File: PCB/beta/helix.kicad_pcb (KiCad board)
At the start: 2 copper layers, 132 x 94 mm, 223 parts, among them J1 MJ-4PP-9, P1 CONN_01X01, P2 CONN_01X01, P3 OLED, P4 LED, P5 ICSP, SW1 SW_PUSH, SW10 SW_PUSH, SW11 SW_PUSH, SW12 SW_PUSH, SW13 SW_PUSH, SW14 SW_PUSH, SW15 SW_PUSH, SW16 SW_PUSH, SW17 SW_PUSH, SW18 SW_PUSH, SW19 SW_PUSH, SW2 SW_PUSH, SW20 SW_PUSH, SW21 SW_PUSH, SW22 SW_PUSH, SW23 SW_PUSH, SW24 SW_PUSH, SW25 SW_PUSH, SW26 SW_PUSH, SW27 SW_PUSH, SW28 SW_PUSH, SW29 SW_PUSH, SW3 SW_PUSH, SW30 SW_PUSH, SW31 SW_PUSH, SW32 SW_PUSH, SW33 Reset, SW4 SW_PUSH, SW5 SW_PUSH, SW6 SW_PUSH, SW7 SW_PUSH, SW8 SW_PUSH, SW9 SW_PUSH, U1 ProMicro, U10 SK6812mini, U11 SK6812mini, U12 SK6812mini, U13 SK6812mini, U14 SK6812mini, U15 SK6812mini, U16 SK6812mini, U17 SK6812mini, U18 SK6812mini, U19 SK6812mini, U2 SK6812mini, U20 SK6812mini, U21 SK6812mini, U22 SK6812mini, U23 SK6812mini, U24 SK6812mini, U25 SK6812mini, U26 SK6812mini, U27 SK6812mini, U28 SK6812mini, U29 SK6812mini, U3 SK6812mini, U30 SK6812mini, U31 SK6812mini, U32 SK6812mini, U33 SK6812mini, U4 SK6812mini, U5 SK6812mini, U6 SK6812mini, U7 SK6812mini, U8 SK6812mini, U9 SK6812mini

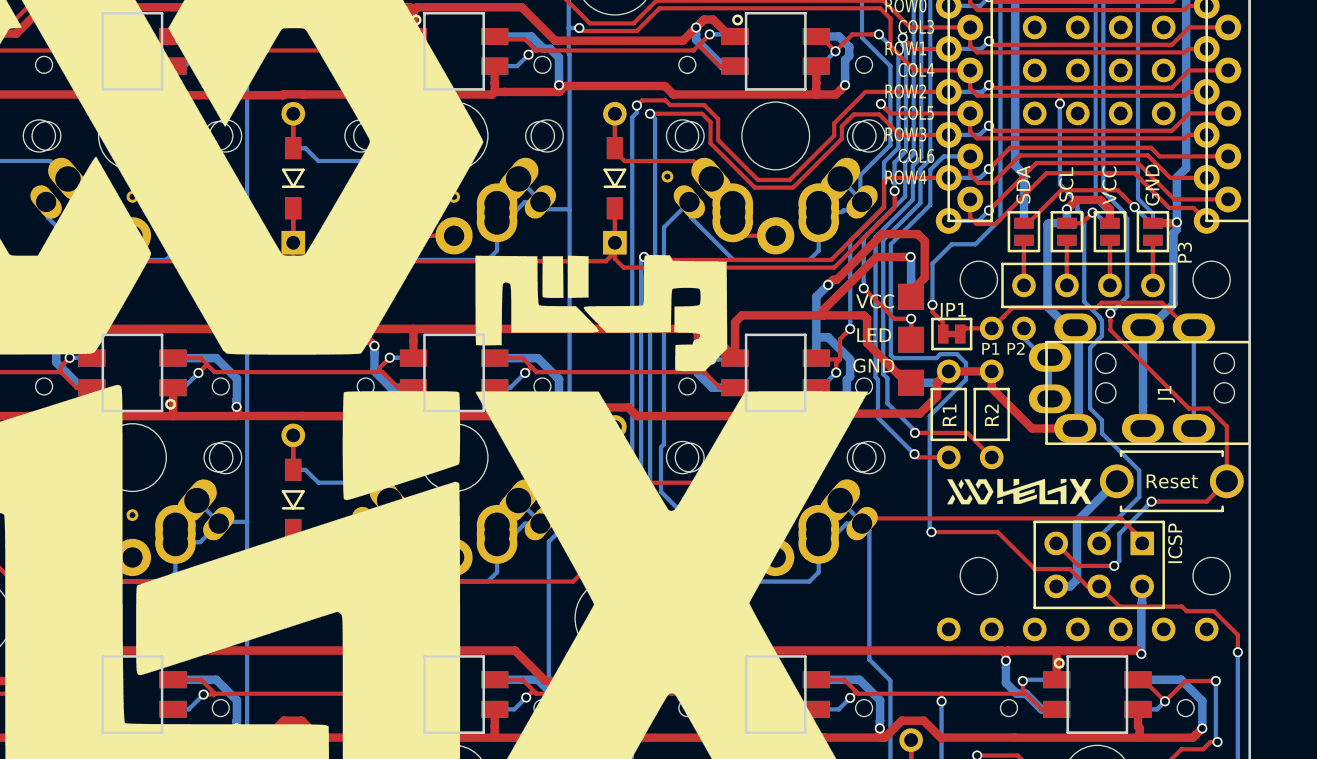
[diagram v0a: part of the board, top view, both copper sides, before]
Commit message: made changes to aux jack (now accepts generic TRS aux cables); pretty much just need to replace/source i2c resistors and we're ready to order
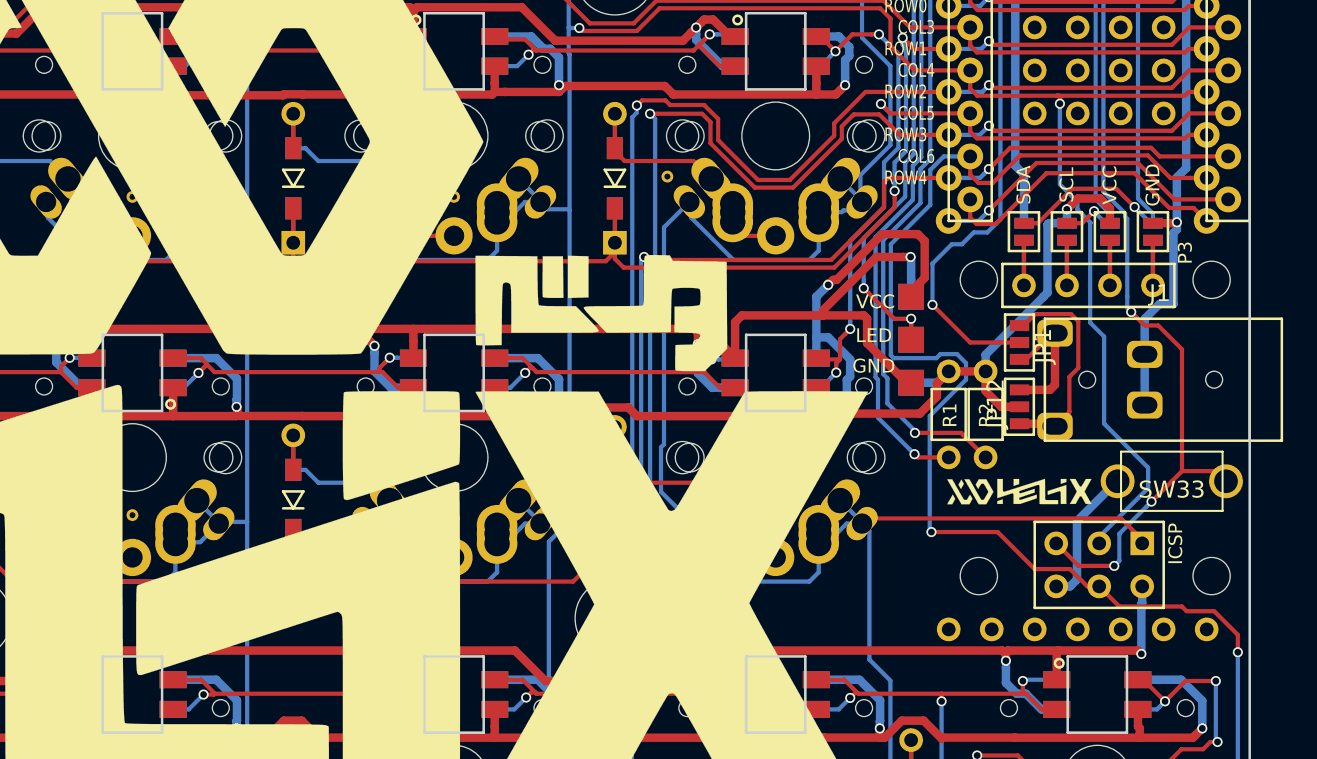
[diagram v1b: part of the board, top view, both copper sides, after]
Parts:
- removed P1, P2: CONN_01X01, MYLIB:1PIN_0.1
- added JP12: Jumper_3_Open, lowprokeeb:jmpr_01x03, F.Cu at (201.4, 88.0)
- J1: value MJ-4PP-9 -> STX-3000; footprint MYLIB_REV:MJ-4PP-9_rev2 -> lowprokeeb:STX-3000
- JP1: value JPC2 -> Jumper_3_Open; footprint MYLIB:JPC2 -> lowprokeeb:jmpr_01x03
- SW33: footprint MYLIB:SW_3.5x6.0_TH -> lowprokeeb:PTS636 SM43 LFS
- moved JP1 4.03 mm to (201.4, 84.2), turned to 270 degrees
- moved J1 2.05 mm to (216.9, 86.4), turned to 180 degrees
- moved R2 0.36 mm to (199.4, 88.5)
- turned SW33 to 0 degrees
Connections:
- JP1 pad 1: data -> Net-(J1-Pad2)
- JP1 pad 2: Net-(J1-PadB) -> data
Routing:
- net Net-(J1-PadB): track 21.1 -> 0.00 mm
- net Net-(J1-Pad2): track 0.00 -> 12.9 mm
- net Net-(J1-Pad3): track 0.00 -> 8.09 mm
- net VCC: track 980.2 -> 973.7 mm
- net Net-(J1-PadA): track 5.03 -> 0.00 mm
- net data: track 52.5 -> 56.3 mm
- net /~RESET: track 71.2 -> 68.9 mm
- net GND: track 863.8 -> 862.7 mm
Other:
- outline, holes or cut-outs redrawn
- board text added: "Modified by sorslyd5"

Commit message: finished sourcing all parts on vanilla helix; need to determine if 1-wire is required for send commands to slave (like neopixels, oled, etc.)
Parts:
- R1: footprint MYLIB:R2 -> Resistor_SMD:R_0603_1608Metric_Pad1.05x0.95mm_HandSolder
- R2: footprint R2 -> Resistor_SMD:R_0603_1608Metric_Pad1.05x0.95mm_HandSolder
- moved R1 2.62 mm to (199.4, 87.0)
- moved JP1 2.27 mm to (199.2, 83.7), turned to 0 degrees
- moved R2 2.16 mm to (197.8, 87.0)
- moved JP12 1.60 mm to (201.4, 86.4)
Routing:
- net Net-(J1-Pad2): track 12.9 -> 17.8 mm
- net /SDA: track 85.1 -> 87.3 mm
- net Net-(J1-Pad3): track 8.09 -> 6.35 mm
- net /SCL: track 71.9 -> 70.2 mm
- net VCC: track 973.7 -> 972.1 mm, vias 43 -> 44
